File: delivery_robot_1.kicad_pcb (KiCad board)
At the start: 4 copper layers, 80 x 90 mm, 114 parts, among them J1 SWD, J10 Port C/D breakout, J11 IMU I2C (STEMMA QT), J12 IMU INT/RST, J13 Pi 5 UART, J14 Pi 5 power, J15 Motor2 encoder, J16 MDD20A PWM2/DIR2/GND, J2 XT30PW-M, J4 BOOT0 jumper, J5 Power test points, J6 MDD20A PWM1/DIR1/GND, J7 Motor1 encoder, J8 Port A breakout, J9 Port B breakout, SW1 RESET, U1 STM32F091RCTx, U2 PTPSM63606RDLR, U3 TPS54202DDCR, U4 TPS7A8101DRBR, U5 PTPSM63606RDLR, U6 USBLC6-4SC6, U7 USBLC6-4SC6, Y3 8MHz

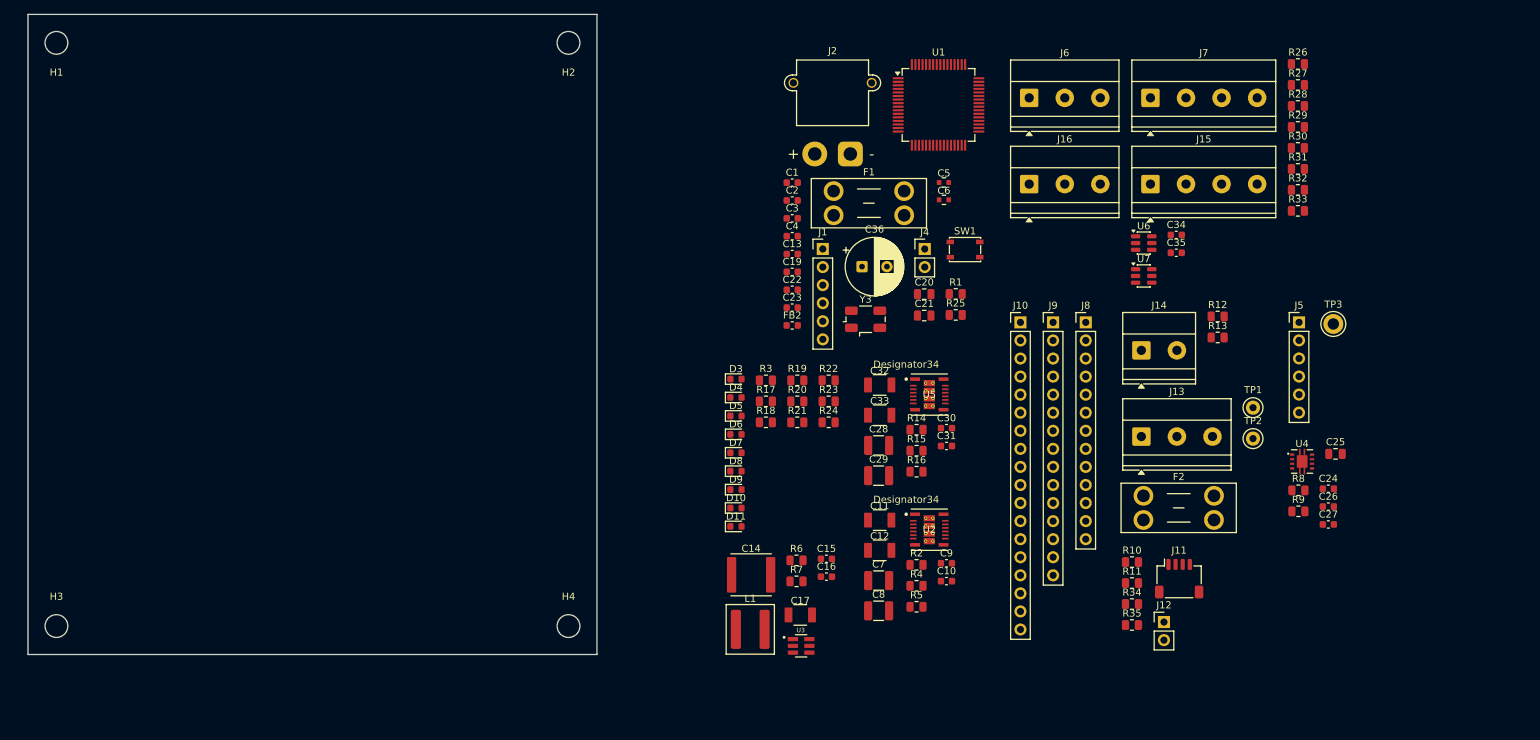
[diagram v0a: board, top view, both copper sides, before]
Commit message: Grow board to 100 x 100 mm and place power input, motor I/O and ESD
Board outline 80 x 90 -> 100 x 100 mm (top-left corner fixed at 85, 50),
bringing part area from ~47 % to ~33 % of the usable board. Holes stay
4 mm in from each corner, locked, each with its 7 x 7 mm keepout:
H1 (4,4), H2 (96,4), H3 (4,96), H4 (96,96). The unplaced parts were
shifted 25 mm right to clear the new outline.

Power input, top-left, as a straight path J2+ -> F1 -> C36:
- J2 XT30: rotated 180 deg so the plug opening faces the left edge
  (it was facing into the board); front 0.5 mm in from the edge
- F1 fuse holder next to J2's + pin; C36 220 uF right after F1's +12V

Motor I/O, bottom-right corner (wire entries face out, 0.5 mm inset):
- Bottom edge: J6 (M1 PWM/DIR/GND), J16 (M2)
- Right edge: J15 (M2 encoder), J7 (M1 encoder)

ESD arrays at their connectors, I/O order matching the connector pins:
- U6 at J6 with C34 (VBUS +3V3); U7 at J7 with C35 (VBUS +5V_SYS)
- 7.2 mm connector-to-array, caps ~2 mm from VBUS; J7 reference moved
  off U7

Also commits the board setup and design rules in the project file.
DRC unchanged at the pre-placement baseline (57, all from unplaced
parts); schematic parity clean.
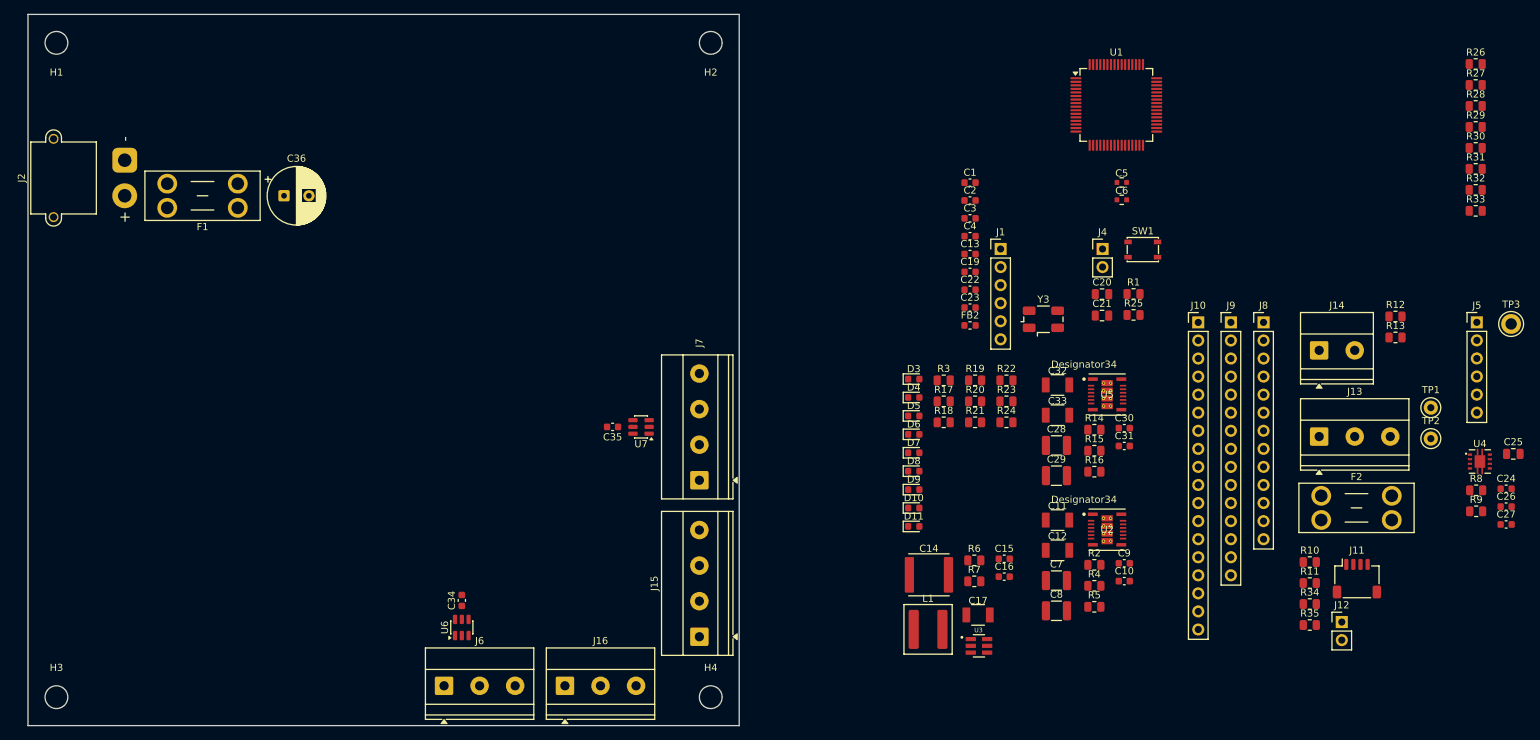
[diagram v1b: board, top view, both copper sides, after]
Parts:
- moved J6 116.6 mm to (143.5, 144.4)
- moved C34 112.8 mm to (146.0, 132.4), turned to 90 degrees
- moved U6 110.1 mm to (146.0, 136.2), turned to 90 degrees
- moved J2 102.0 mm to (98.6, 70.5), turned to 90 degrees
- moved J16 96.1 mm to (160.5, 144.4)
- moved J15 89.8 mm to (179.4, 137.5), turned to 90 degrees
- moved F1 83.8 mm to (114.5, 77.2), turned to 180 degrees
- moved J7 83.1 mm to (179.4, 115.5), turned to 90 degrees
- moved C35 83.0 mm to (167.2, 108.0), turned to 180 degrees
- moved C36 81.9 mm to (121.0, 75.5)
- moved U7 73.8 mm to (171.2, 108.0), turned to 180 degrees
- moved J11 25.0 mm to (271.9, 129.3)
- moved J12 25.0 mm to (269.7, 135.4)
- moved J13 25.0 mm to (266.5, 109.4)
- moved J14 25.0 mm to (266.5, 97.2)
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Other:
- board size 80 x 90 mm -> 100 x 100 mm
